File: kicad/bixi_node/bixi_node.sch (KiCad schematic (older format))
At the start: 1 part

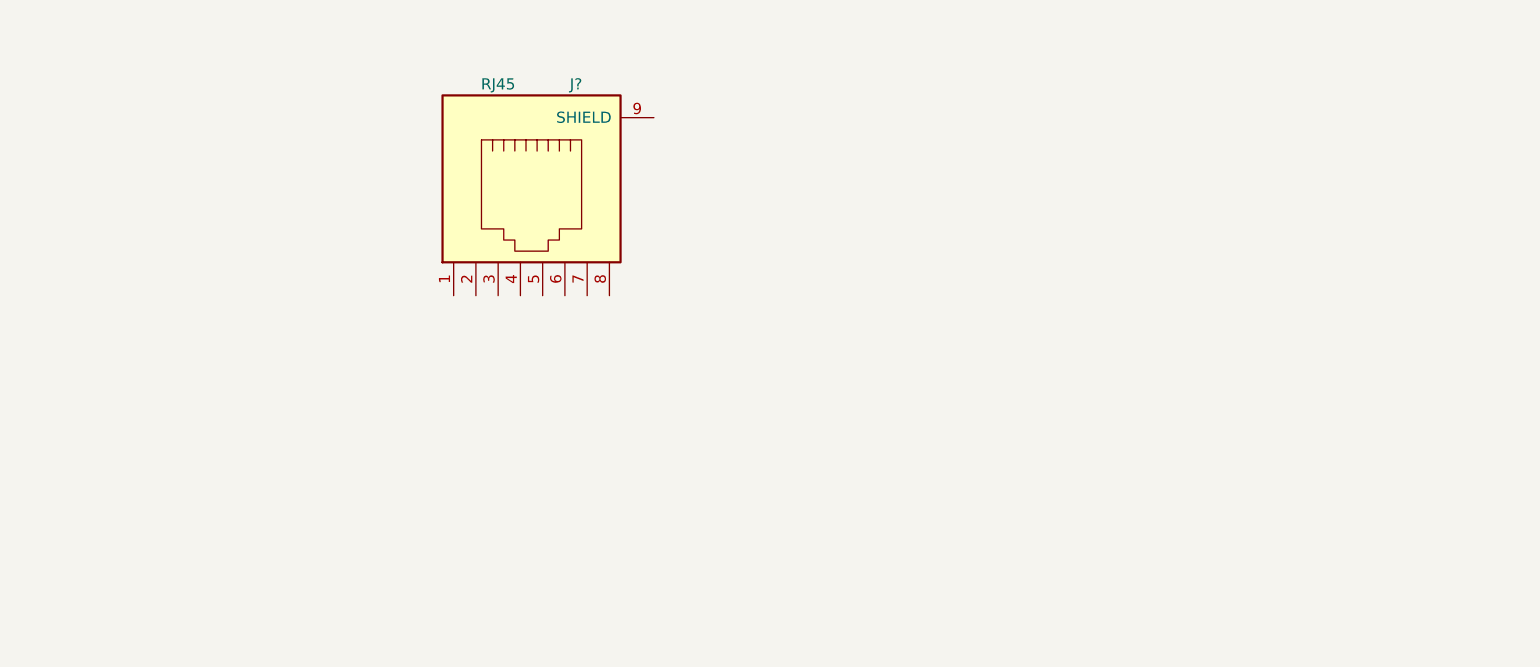
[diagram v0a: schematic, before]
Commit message: updated controller layout
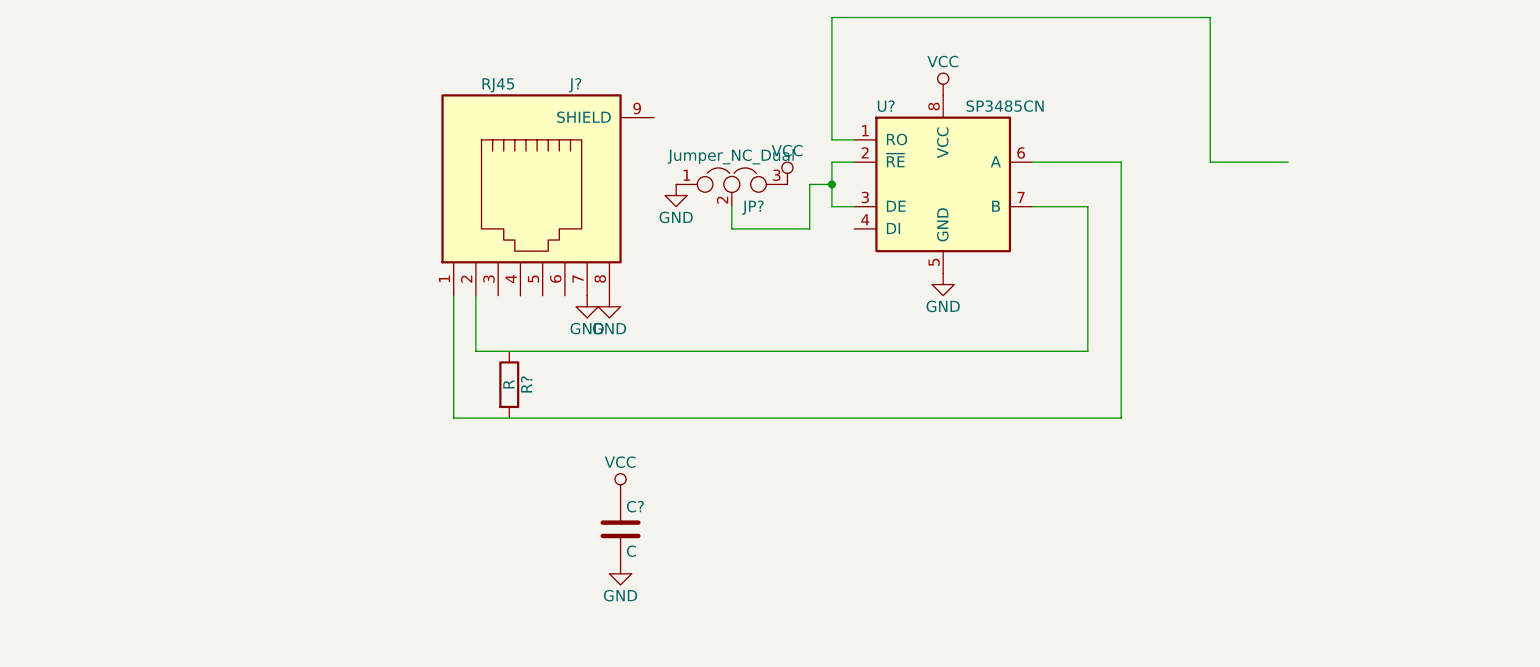
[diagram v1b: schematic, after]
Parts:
- added C?: C, symbol C
- added JP?: Jumper_NC_Dual, symbol Jumper_NC_Dual
- added R?: R, symbol R
- added U?: SP3485CN, Housings_SOIC:SOIC-8_3.9x4.9mm_Pitch1.27mm, symbol SP3485CN
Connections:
- net labels added: GND, VCC
- wire segments 0 -> 20
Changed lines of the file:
@@
 LIBS:contrib
 LIBS:valves
+LIBS:bixi_node-cache
 EELAYER 25 0
 EELAYER END
@@
 	1    0    0    -1
 $EndComp
+$Comp
+L SP3485CN U?
+U 1 1 58CE0617
+P 5800 3300
+F 0 "U?" H 5500 3650 50  0000 L CNN
+F 1 "SP3485CN" H 5900 3650 50  0000 L CNN
+F 2 "Housings_SOIC:SOIC-8_3.9x4.9mm_Pitch1.27mm" H 6850 2950 50  0001 C CIN
+F 3 "" H 5800 3300 50  0000 C CNN
+	1    5800 3300
+	1    0    0    -1
+$EndComp
+$Comp
+L GND #PWR?
+U 1 1 58CE067C
+P 5800 3700
+F 0 "#PWR?" H 5800 3450 50  0001 C CNN
+F 1 "GND" H 5800 3550 50  0000 C CNN
+F 2 "" H 5800 3700 50  0000 C CNN
+F 3 "" H 5800 3700 50  0000 C CNN
+	1    5800 3700
+	1    0    0    -1
+$EndComp
+$Comp
+L GND #PWR?
+U 1 1 58CE0696
+P 4200 3800
+F 0 "#PWR?" H 4200 3550 50  0001 C CNN
+F 1 "GND" H 4200 3650 50  0000 C CNN
+F 2 "" H 4200 3800 50  0000 C CNN
+F 3 "" H 4200 3800 50  0000 C CNN
+	1    4200 3800
+	1    0    0    -1
+$EndComp
+$Comp
+L GND #PWR?
+U 1 1 58CE06B0
+P 4300 3800
+F 0 "#PWR?" H 4300 3550 50  0001 C CNN
+F 1 "GND" H 4300 3650 50  0000 C CNN
+F 2 "" H 4300 3800 50  0000 C CNN
+F 3 "" H 4300 3800 50  0000 C CNN
+	1    4300 3800
+	1    0    0    -1
+$EndComp
+$Comp
+L VCC #PWR?
+U 1 1 58CE06CA
+P 5800 2900
+F 0 "#PWR?" H 5800 2750 50  0001 C CNN
+F 1 "VCC" H 5800 3050 50  0000 C CNN
+F 2 "" H 5800 2900 50  0000 C CNN
+F 3 "" H 5800 2900 50  0000 C CNN
+	1    5800 2900
+	1    0    0    -1
+$EndComp
+$Comp
+L R R?
+U 1 1 58CE071A
+P 3850 4200
+F 0 "R?" V 3930 4200 50  0000 C CNN
+F 1 "R" V 3850 4200 50  0000 C CNN
+F 2 "" V 3780 4200 50  0000 C CNN
+F 3 "" H 3850 4200 50  0000 C CNN
+	1    3850 4200
+	1    0    0    -1
+$EndComp
+$Comp
+L C C?
+U 1 1 58CE0786
+P 4350 4850
+F 0 "C?" H 4375 4950 50  0000 L CNN
+F 1 "C" H 4375 4750 50  0000 L CNN
+F 2 "" H 4388 4700 50  0000 C CNN
+F 3 "" H 4350 4850 50  0000 C CNN
+	1    4350 4850
+	1    0    0    -1
+$EndComp
+$Comp
+L VCC #PWR?
+U 1 1 58CE07F1
+P 4350 4700
+F 0 "#PWR?" H 4350 4550 50  0001 C CNN
+F 1 "VCC" H 4350 4850 50  0000 C CNN
+F 2 "" H 4350 4700 50  0000 C CNN
+F 3 "" H 4350 4700 50  0000 C CNN
+	1    4350 4700
+	1    0    0    -1
+$EndComp
+$Comp
+L GND #PWR?
+U 1 1 58CE0C7F
+P 4350 5000
+F 0 "#PWR?" H 4350 4750 50  0001 C CNN
+F 1 "GND" H 4350 4850 50  0000 C CNN
+F 2 "" H 4350 5000 50  0000 C CNN
+F 3 "" H 4350 5000 50  0000 C CNN
+	1    4350 5000
+	1    0    0    -1
+$EndComp
+$Comp
+L Jumper_NC_Dual JP?
+U 1 1 58CE0E18
+P 4850 3300
+F 0 "JP?" H 4900 3200 50  0000 L CNN
+F 1 "Jumper_NC_Dual" H 4850 3400 50  0000 C BNN
+F 2 "" H 4850 3300 50  0000 C CNN
+F 3 "" H 4850 3300 50  0000 C CNN
+	1    4850 3300
+	1    0    0    -1
+$EndComp
+Wire Wire Line
+	3700 3800 3700 4050
+Wire Wire Line
+	3700 4050 6450 4050
+Wire Wire Line
+	6450 4050 6450 3400
+Wire Wire Line
+	6450 3400 6200 3400
+Wire Wire Line
+	3600 3800 3600 4350
+Wire Wire Line
+	3600 4350 6600 4350
+Wire Wire Line
+	6600 4350 6600 3200
+Wire Wire Line
+	6600 3200 6200 3200
+Wire Wire Line
+	5400 3400 5300 3400
+Wire Wire Line
+	5300 3400 5300 3200
+Wire Wire Line
+	5300 3200 5400 3200
+Wire Wire Line
+	5300 3300 5200 3300
+Wire Wire Line
+	5200 3300 5200 3500
+Wire Wire Line
+	5200 3500 4850 3500
+Wire Wire Line
+	4850 3500 4850 3400
+Connection ~ 5300 3300
+$Comp
+L GND #PWR?
+U 1 1 58CE0E7E
+P 4600 3300
+F 0 "#PWR?" H 4600 3050 50  0001 C CNN
+F 1 "GND" H 4600 3150 50  0000 C CNN
+F 2 "" H 4600 3300 50  0000 C CNN
+F 3 "" H 4600 3300 50  0000 C CNN
+	1    4600 3300
+	1    0    0    -1
+$EndComp
+$Comp
+L VCC #PWR?
+U 1 1 58CE0EA1
+P 5100 3300
+F 0 "#PWR?" H 5100 3150 50  0001 C CNN
+F 1 "VCC" H 5100 3450 50  0000 C CNN
+F 2 "" H 5100 3300 50  0000 C CNN
+F 3 "" H 5100 3300 50  0000 C CNN
+	1    5100 3300
+	1    0    0    -1
+$EndComp
+Wire Wire Line
+	5400 3100 5300 3100
+Wire Wire Line
+	5300 3100 5300 2550
+Wire Wire Line
+	5300 2550 7000 2550
+Wire Wire Line
+	7000 2550 7000 3200
+Wire Wire Line
+	7000 3200 7350 3200
 $EndSCHEMATC

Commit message: controller and receiver boards almost done for v1
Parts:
- removed JP?: Jumper_NC_Dual, symbol Jumper_NC_Dual
- added CON1: BARREL_JACK, custom:BARREL_JACK_2PIN, symbol BARREL_JACK
- added P1: CONN_01X03, custom:PAD_3X_OVAL, symbol CONN_01X03
- C1: renamed from C?; footprint (none) -> Resistors_THT:Resistor_Horizontal_RM7mm
- J1: renamed from J?; footprint (none) -> Connectors:RJ45_8
- R1: renamed from R?; footprint (none) -> Resistors_THT:Resistor_Horizontal_RM7mm
- U1: renamed from U?; footprint Housings_SOIC:SOIC-8_3.9x4.9mm_Pitch1.27mm -> Housings_DIP:DIP-8_W7.62mm
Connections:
- wire segments 20 -> 18
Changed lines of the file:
@@
 $EndDescr
 $Comp
-L RJ45 J?
+L RJ45 J1
 U 1 1 58CDFC74
 P 3950 3350
-F 0 "J?" H 4150 3850 50  0000 C CNN
+F 0 "J1" H 4150 3850 50  0000 C CNN
 F 1 "RJ45" H 3800 3850 50  0000 C CNN
-F 2 "" H 3950 3350 50  0000 C CNN
+F 2 "Connectors:RJ45_8" H 3950 3350 50  0001 C CNN
 F 3 "" H 3950 3350 50  0000 C CNN
 	1    3950 3350
@@
 $EndComp
 $Comp
-L SP3485CN U?
+L SP3485CN U1
 U 1 1 58CE0617
 P 5800 3300
-F 0 "U?" H 5500 3650 50  0000 L CNN
+F 0 "U1" H 5500 3650 50  0000 L CNN
 F 1 "SP3485CN" H 5900 3650 50  0000 L CNN
-F 2 "Housings_SOIC:SOIC-8_3.9x4.9mm_Pitch1.27mm" H 6850 2950 50  0001 C CIN
+F 2 "Housings_DIP:DIP-8_W7.62mm" H 6850 2950 50  0001 C CIN
 F 3 "" H 5800 3300 50  0000 C CNN
 	1    5800 3300
@@
 $EndComp
 $Comp
-L GND #PWR?
+L GND #PWR01
 U 1 1 58CE067C
 P 5800 3700
-F 0 "#PWR?" H 5800 3450 50  0001 C CNN
+F 0 "#PWR01" H 5800 3450 50  0001 C CNN
 F 1 "GND" H 5800 3550 50  0000 C CNN
 F 2 "" H 5800 3700 50  0000 C CNN
@@
 $EndComp
 $Comp
-L GND #PWR?
+L GND #PWR02
 U 1 1 58CE0696
 P 4200 3800
-F 0 "#PWR?" H 4200 3550 50  0001 C CNN
+F 0 "#PWR02" H 4200 3550 50  0001 C CNN
 F 1 "GND" H 4200 3650 50  0000 C CNN
 F 2 "" H 4200 3800 50  0000 C CNN
@@
 $EndComp
 $Comp
-L GND #PWR?
+L GND #PWR03
 U 1 1 58CE06B0
 P 4300 3800
-F 0 "#PWR?" H 4300 3550 50  0001 C CNN
+F 0 "#PWR03" H 4300 3550 50  0001 C CNN
 F 1 "GND" H 4300 3650 50  0000 C CNN
 F 2 "" H 4300 3800 50  0000 C CNN
@@
 $EndComp
 $Comp
-L VCC #PWR?
+L VCC #PWR04
 U 1 1 58CE06CA
 P 5800 2900
-F 0 "#PWR?" H 5800 2750 50  0001 C CNN
+F 0 "#PWR04" H 5800 2750 50  0001 C CNN
 F 1 "VCC" H 5800 3050 50  0000 C CNN
 F 2 "" H 5800 2900 50  0000 C CNN
@@
 $EndComp
 $Comp
-L R R?
+L R R1
 U 1 1 58CE071A
 P 3850 4200
-F 0 "R?" V 3930 4200 50  0000 C CNN
+F 0 "R1" V 3930 4200 50  0000 C CNN
 F 1 "R" V 3850 4200 50  0000 C CNN
-F 2 "" V 3780 4200 50  0000 C CNN
+F 2 "Resistors_THT:Resistor_Horizontal_RM7mm" V 3780 4200 50  0001 C CNN
 F 3 "" H 3850 4200 50  0000 C CNN
 	1    3850 4200
@@
 $EndComp
 $Comp
-L C C?
+L C C1
 U 1 1 58CE0786
 P 4350 4850
-F 0 "C?" H 4375 4950 50  0000 L CNN
+F 0 "C1" H 4375 4950 50  0000 L CNN
 F 1 "C" H 4375 4750 50  0000 L CNN
-F 2 "" H 4388 4700 50  0000 C CNN
+F 2 "Resistors_THT:Resistor_Horizontal_RM7mm" H 4388 4700 50  0001 C CNN
 F 3 "" H 4350 4850 50  0000 C CNN
 	1    4350 4850
@@
 $EndComp
 $Comp
-L VCC #PWR?
+L VCC #PWR05
 U 1 1 58CE07F1
 P 4350 4700
-F 0 "#PWR?" H 4350 4550 50  0001 C CNN
+F 0 "#PWR05" H 4350 4550 50  0001 C CNN
 F 1 "VCC" H 4350 4850 50  0000 C CNN
 F 2 "" H 4350 4700 50  0000 C CNN
@@
 $EndComp
 $Comp
-L GND #PWR?
+L GND #PWR06
 U 1 1 58CE0C7F
 P 4350 5000
-F 0 "#PWR?" H 4350 4750 50  0001 C CNN
+F 0 "#PWR06" H 4350 4750 50  0001 C CNN
 F 1 "GND" H 4350 4850 50  0000 C CNN
 F 2 "" H 4350 5000 50  0000 C CNN
@@
 	1    0    0    -1
 $EndComp
-$Comp
-L Jumper_NC_Dual JP?
-U 1 1 58CE0E18
-P 4850 3300
-F 0 "JP?" H 4900 3200 50  0000 L CNN
-F 1 "Jumper_NC_Dual" H 4850 3400 50  0000 C BNN
-F 2 "" H 4850 3300 50  0000 C CNN
-F 3 "" H 4850 3300 50  0000 C CNN
-	1    4850 3300
-	1    0    0    -1
-$EndComp
 Wire Wire Line
 	3700 3800 3700 4050
@@
 Wire Wire Line
 	5300 3200 5400 3200
-Wire Wire Line
-	5300 3300 5200 3300
-Wire Wire Line
-	5200 3300 5200 3500
-Wire Wire Line
-	5200 3500 4850 3500
-Wire Wire Line
-	4850 3500 4850 3400
 Connection ~ 5300 3300
-$Comp
-L GND #PWR?
+Wire Wire Line
+	5400 3100 5300 3100
+Wire Wire Line
+	5300 3100 5300 2550
+Wire Wire Line
+	5300 2550 7000 2550
+Wire Wire Line
+	7000 2550 7000 3200
+Wire Wire Line
+	7000 3200 7350 3200
+$Comp
+L GND #PWR07
 U 1 1 58CE0E7E
-P 4600 3300
-F 0 "#PWR?" H 4600 3050 50  0001 C CNN
-F 1 "GND" H 4600 3150 50  0000 C CNN
-F 2 "" H 4600 3300 50  0000 C CNN
-F 3 "" H 4600 3300 50  0000 C CNN
-	1    4600 3300
-	1    0    0    -1
-$EndComp
-$Comp
-L VCC #PWR?
-U 1 1 58CE0EA1
 P 5100 3300
-F 0 "#PWR?" H 5100 3150 50  0001 C CNN
-F 1 "VCC" H 5100 3450 50  0000 C CNN
+F 0 "#PWR07" H 5100 3050 50  0001 C CNN
+F 1 "GND" H 5100 3150 50  0000 C CNN
 F 2 "" H 5100 3300 50  0000 C CNN
 F 3 "" H 5100 3300 50  0000 C CNN
@@
 $EndComp
 Wire Wire Line
-	5400 3100 5300 3100
-Wire Wire Line
-	5300 3100 5300 2550
-Wire Wire Line
-	5300 2550 7000 2550
-Wire Wire Line
-	7000 2550 7000 3200
-Wire Wire Line
-	7000 3200 7350 3200
+	5300 3300 5100 3300
+$Comp
+L VCC #PWR08
+U 1 1 58D6B5B6
+P 7350 3100
+F 0 "#PWR08" H 7350 2950 50  0001 C CNN
+F 1 "VCC" H 7350 3250 50  0000 C CNN
+F 2 "" H 7350 3100 50  0000 C CNN
+F 3 "" H 7350 3100 50  0000 C CNN
+	1    7350 3100
+	1    0    0    -1
+$EndComp
+$Comp
+L GND #PWR09
+U 1 1 58D6B5DA
+P 7350 3300
+F 0 "#PWR09" H 7350 3050 50  0001 C CNN
+F 1 "GND" H 7350 3150 50  0000 C CNN
+F 2 "" H 7350 3300 50  0000 C CNN
+F 3 "" H 7350 3300 50  0000 C CNN
+	1    7350 3300
+	1    0    0    -1
+$EndComp
+$Comp
+L BARREL_JACK CON1
+U 1 1 58D6B605
+P 5400 4800
+F 0 "CON1" H 5400 5050 50  0000 C CNN
+F 1 "BARREL_JACK" H 5400 4600 50  0000 C CNN
+F 2 "custom:BARREL_JACK_2PIN" H 5400 4800 50  0001 C CNN
+F 3 "" H 5400 4800 50  0000 C CNN
+	1    5400 4800
+	1    0    0    -1
+$EndComp
+$Comp
+L GND #PWR010
+U 1 1 58D6B6AE
+P 5700 4900
+F 0 "#PWR010" H 5700 4650 50  0001 C CNN
+F 1 "GND" H 5700 4750 50  0000 C CNN
+F 2 "" H 5700 4900 50  0000 C CNN
+F 3 "" H 5700 4900 50  0000 C CNN
+	1    5700 4900
+	1    0    0    -1
+$EndComp
+Wire Wire Line
+	5700 4800 5700 4900
+$Comp
+L VCC #PWR011
+U 1 1 58D6B70F
+P 5700 4700
+F 0 "#PWR011" H 5700 4550 50  0001 C CNN
+F 1 "VCC" H 5700 4850 50  0000 C CNN
+F 2 "" H 5700 4700 50  0000 C CNN
+F 3 "" H 5700 4700 50  0000 C CNN
+	1    5700 4700
+	1    0    0    -1
+$EndComp
+$Comp
+L CONN_01X03 P1
+U 1 1 58D6C384
+P 7550 3200
+F 0 "P1" H 7550 3400 50  0000 C CNN
+F 1 "CONN_01X03" V 7650 3200 50  0000 C CNN
+F 2 "custom:PAD_3X_OVAL" H 7550 3200 50  0001 C CNN
+F 3 "" H 7550 3200 50  0000 C CNN
+	1    7550 3200
+	1    0    0    -1
+$EndComp
+Connection ~ 3850 4050
+Connection ~ 3850 4350
 $EndSCHEMATC

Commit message: keep-out area for terminal block, finalized node pcb
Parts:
- removed CON1: BARREL_JACK, custom:BARREL_JACK_2PIN, symbol BARREL_JACK
- added J2: Screw_Terminal_1x02, custom:HB9500-2P, symbol Screw_Terminal_1x02
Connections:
- wire segments 18 -> 17
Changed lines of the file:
@@
-$EndComp
-$Comp
-L BARREL_JACK CON1
-U 1 1 58D6B605
-P 5400 4800
-F 0 "CON1" H 5400 5050 50  0000 C CNN
-F 1 "BARREL_JACK" H 5400 4600 50  0000 C CNN
-F 2 "custom:BARREL_JACK_2PIN" H 5400 4800 50  0001 C CNN
-F 3 "" H 5400 4800 50  0000 C CNN
-	1    5400 4800
-	1    0    0    -1
 $EndComp
 $Comp
@@
 	1    0    0    -1
 $EndComp
-Wire Wire Line
-	5700 4800 5700 4900
 $Comp
 L VCC #PWR011
@@
 Connection ~ 3850 4050
 Connection ~ 3850 4350
+$Comp
+L Screw_Terminal_1x02 J2
+U 1 1 58E151AB
+P 5500 4800
+F 0 "J2" H 5500 5050 50  0000 C TNN
+F 1 "Screw_Terminal_1x02" V 5350 4800 50  0000 C TNN
+F 2 "custom:HB9500-2P" H 5500 4575 50  0001 C CNN
+F 3 "" H 5475 4800 50  0001 C CNN
+	1    5500 4800
+	1    0    0    -1
+$EndComp
 $EndSCHEMATC
